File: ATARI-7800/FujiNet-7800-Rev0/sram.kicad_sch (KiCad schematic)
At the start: 3 parts, among them U2 AS6C4008-55TIN

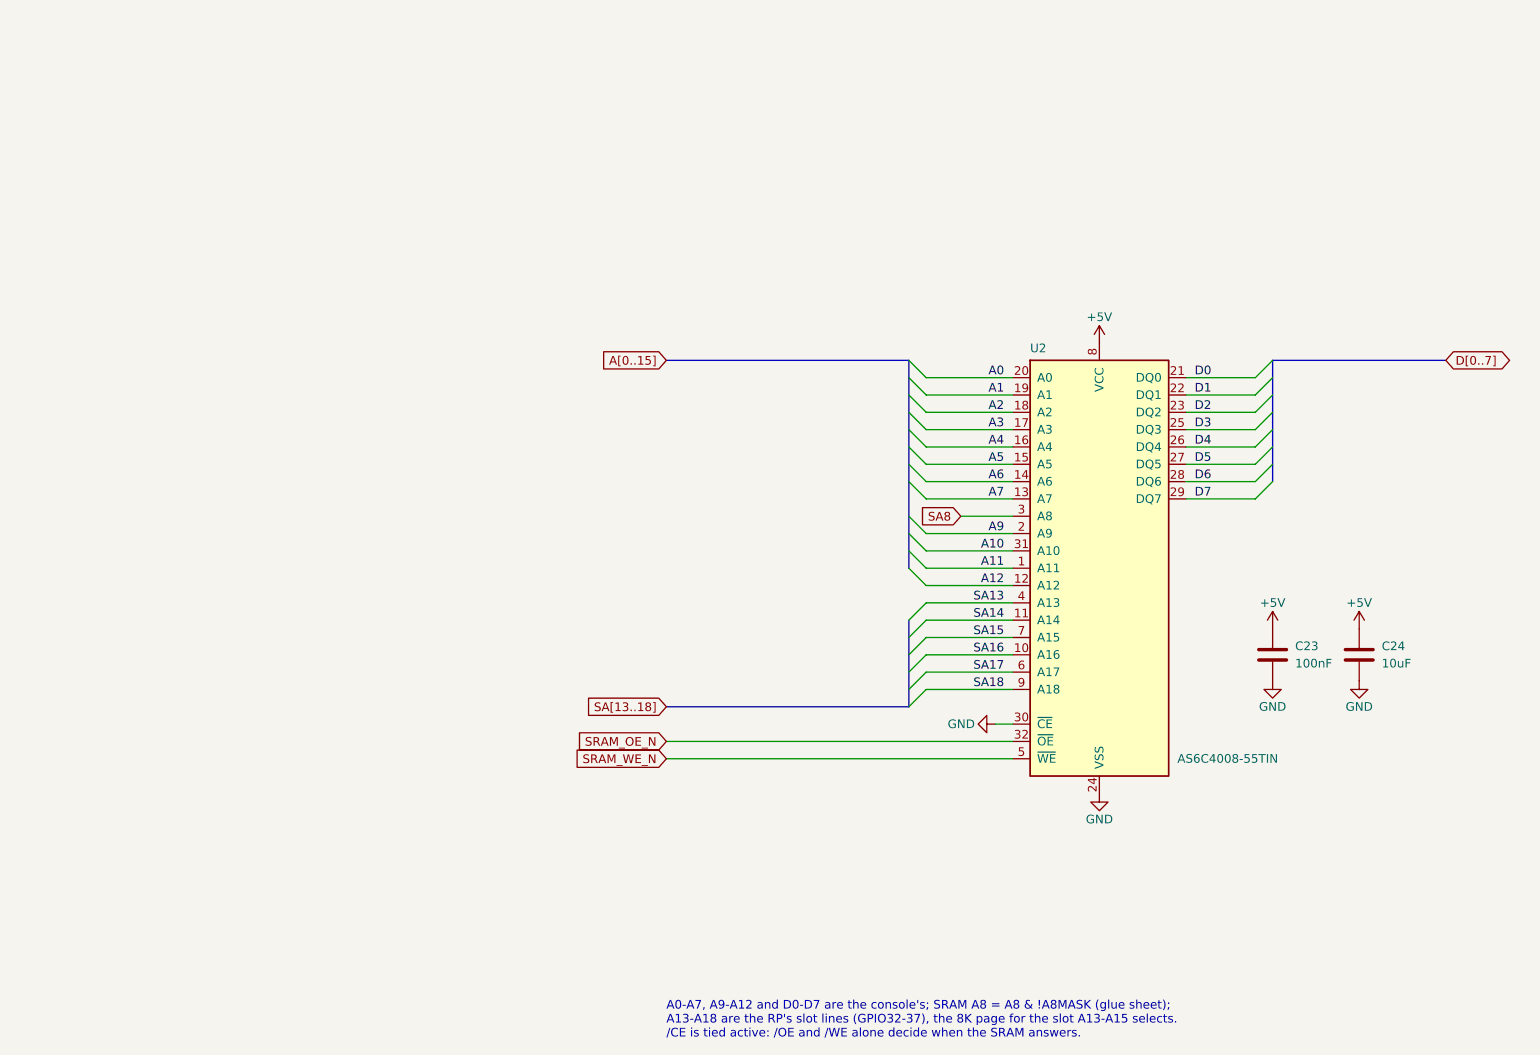
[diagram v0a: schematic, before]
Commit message: ATARI-7800 Rev0: fix the edge, audit the circuit, redraw from the slot, place the board
Edge (board-killer in the schematic-only footprint): the 7800 edge has 18
positions at 2.54 mm with key slots at 3 and 16 for the console's plastic
keys. Pins 1, 2, 15, 16 (and 32, 31, 18, 17) sat one pitch inward, on the
key positions, with no slots and a 42.6 mm tab. tools/edge_geom.py now holds
the geometry (47.0 mm tab, slots centred on +-16.51, 2.4 x 10 mm);
tools/audit/edge_orientation.py checks it against Otaku-flash, tdididit's
boards, the a78-devcart gerbers and this repo's working FujiPlusCart
prototype gerbers (faces and power fingers).

Circuit (console research: Atari C025231 schematic, GCC1702B MARIA spec):
- 4.7k pull-downs on ROM_EN / RAM_EN / A8MASK (RP2350-E9)
- 1k at the /HALT finger (MARIA's HALT is a weak MOS output)
- 10 uF at the console 5V finger; bring-up test pads
- TS-1187A buttons and WS2812C-2020-V1 (the TL3342 and WS2812B-2020
  had 5 in stock at JLC); manufacturer fields for PCBWay
No glue change: R/W is pulled up during MARIA DMA, and the console gates
A15/A14/A12 low while its BIOS is mapped, so CARTSEL never fights it.

Schematic: SMS Rev0's hierarchy (wired root block diagram, hierarchical
labels, netlist parity); sheets in flow order from the slot; the glue
redrawn as a left-to-right gate-depth diagram; references renumbered
from the slot. ERC 0, check_nets 383/383, check_glue 4096/4096.

Board (not yet routed): SMS Rev0's 6-layer pipeline ported. A 72.4 x 115 mm
outline: the stock T-bar width on a 47 x 16.5 mm tab, with the key slots
cut in. Placement variant A (RP over the address fingers, SRAM over the
data fingers): unrouted DRC 0 errors, parity 0, check_vias 0. Shell:
case/FujiNet-7800-Shell.scad. README still describes the old board.

Co-Authored-By: Claude Opus 5.5 <noreply@anthropic.com>
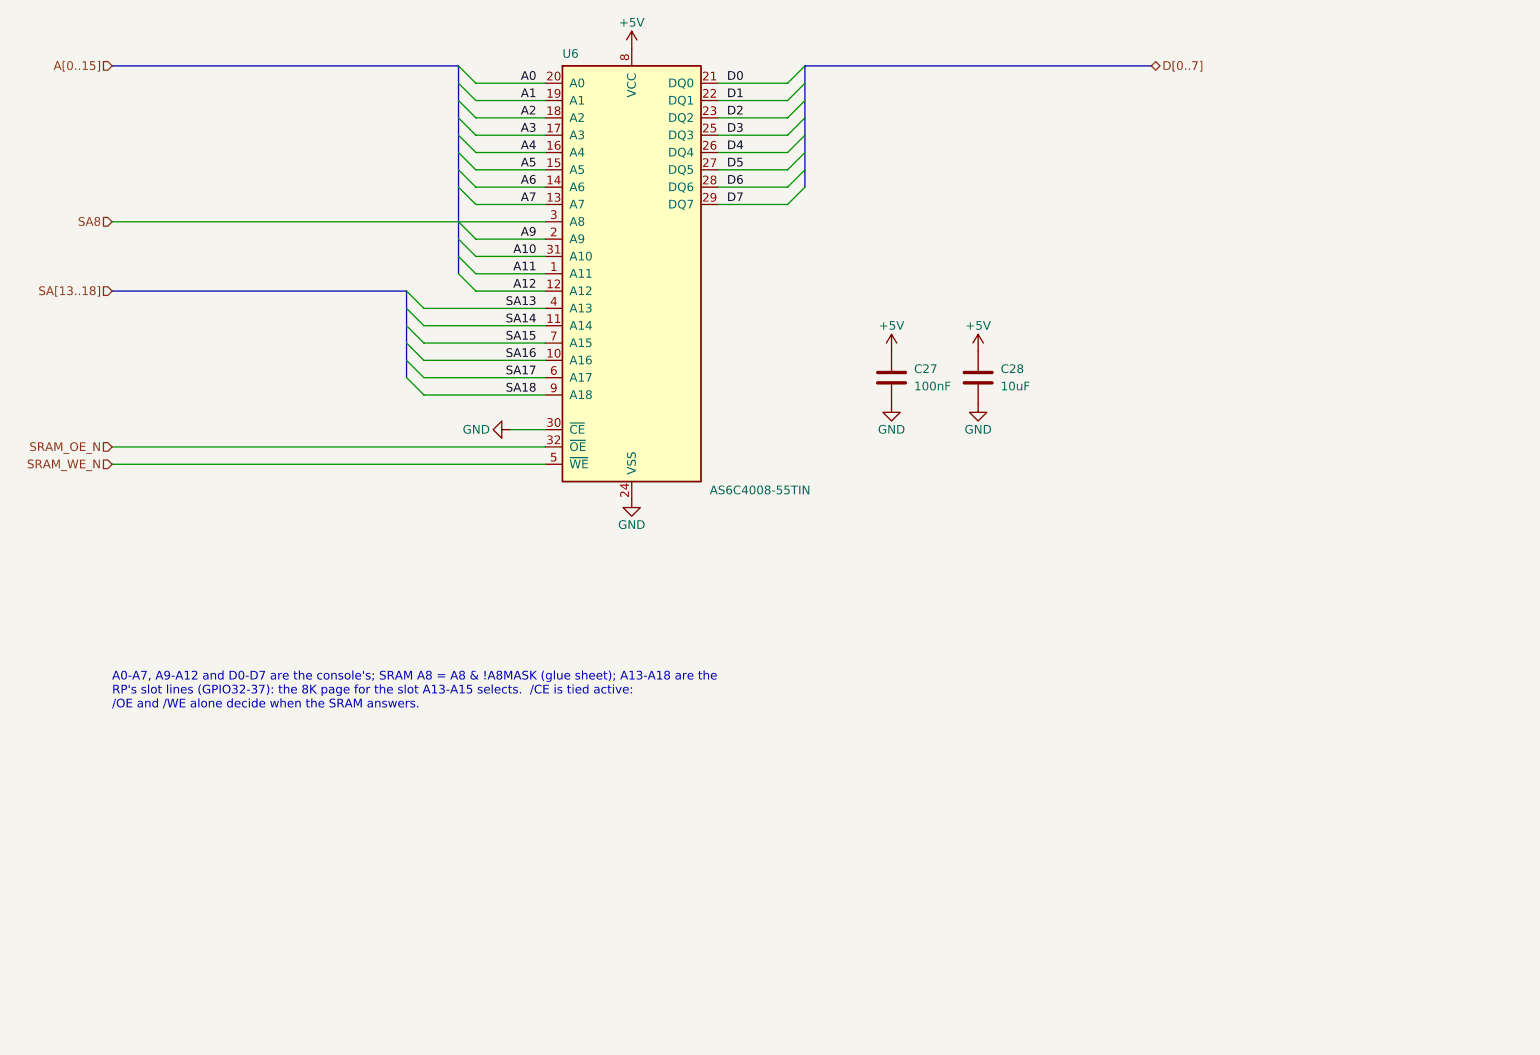
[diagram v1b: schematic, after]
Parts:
- removed C23: 100nF, FujiNet-7800:C_0603_1608Metric, symbol Device:C
- removed C24: 10uF, FujiNet-7800:C_0603_1608Metric, symbol Device:C
- removed U2: AS6C4008-55TIN, FujiNet-7800:TSOP-I-32_18.4x8mm_P0.5mm, symbol FujiNet-7800:AS6C4008-55TIN
- added C27: 100nF, FujiNet-7800:C_0603_1608Metric, symbol Device:C
- added C28: 10uF, FujiNet-7800:C_0603_1608Metric, symbol Device:C
- added U6: AS6C4008-55TIN, FujiNet-7800:TSOP-I-32_18.4x8mm_P0.5mm, symbol FujiNet-7800:AS6C4008-55TIN
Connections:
- net +5V: now also C27.1, C28.1, U6.8 (VCC)
- net A0: now also U6.20 (A0)
- net A1: now also U6.19 (A1)
- net A10: now also U6.31 (A10)
- net A11: now also U6.1 (A11)
- net A12: now also U6.12 (A12)
- net A2: now also U6.18 (A2)
- net A3: now also U6.17 (A3)
- net A4: now also U6.16 (A4)
- net A5: now also U6.15 (A5)
- net A6: now also U6.14 (A6)
- net A7: now also U6.13 (A7)
- net A9: now also U6.2 (A9)
- net D0: now also U6.21 (DQ0)
- net D1: now also U6.22 (DQ1)
- net D2: now also U6.23 (DQ2)
- net D3: now also U6.25 (DQ3)
- net D4: now also U6.26 (DQ4)
- net D5: now also U6.27 (DQ5)
- net D6: now also U6.28 (DQ6)
- net D7: now also U6.29 (DQ7)
- net GND: now also C27.2, C28.2, U6.24 (VSS), U6.30 (~{CE})
- net SA13: now also U6.4 (A13)
- net SA14: now also U6.11 (A14)
- net SA15: now also U6.7 (A15)
- net SA16: now also U6.10 (A16)
- net SA17: now also U6.6 (A17)
- net SA18: now also U6.9 (A18)
- net SA8: now also U6.3 (A8)
- net SRAM_OE_N: now also U6.32 (~{OE})
- net SRAM_WE_N: now also U6.5 (~{WE})
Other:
- note added: "A0-A7, A9-A12 and D0-D7 are the console's; SRAM A8 = A8 & !A8MASK (glue sheet); A13-A18 are the RP's slot lines (GPIO32-37): the 8K page for the slot A13-A15 selects. /CE is tied active: /OE and /WE alone decide when the SRAM answers."
- note removed: "A0-A7, A9-A12 and D0-D7 are the console's; SRAM A8 = A8 & !A8MASK (glue sheet); A13-A18 are the RP's slot lines (GPIO32-37), the 8K page for the slot A13-A15 selects. /CE is tied active: /OE and /WE alone decide when the SRAM answers."
